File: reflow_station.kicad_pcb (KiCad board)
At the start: 6 copper layers, 180 x 110 mm, 271 parts, among them IC1 MP100LGN-Z, IC2 AMC23C10DWVR, J1 1731734, J10 USB_A, J11 USB_C_Receptacle_USB2.0_16P, J12 Conn_ARM_JTAG_SWD_10, J13 F52Q-1A7H1-11015, J2 1707027, J3 1707027, J4 1707027, J5 1707027, J6 DG301-5.0-02P-12-00A_H_, J7 DG301-5.0-02P-12-00A_H_, J8 DG301-5.0-02P-12-00A_H_, J9 DG301-5.0-02P-12-00A_H_, M1 Fan_CPU_4pin, M2 Fan_CPU_4pin, M3 Fan_CPU_4pin, M4 Fan_CPU_4pin, Q1 BTA16-600B, Q2 BTA16-600B, Q3 BTA16-600B, Q4 BTA16-600B, Q5 KSC1815YTA, SW2 SW_SPST, SW3 SW_SPST, SW4 SW_SPST, SW5 SW_DIP_x08, SW6 SW_Push, SW7 SW_SPDT, SW8 SW_SPDT, U1 TPS82130, U10 TPS2051BDBVR, U11 RCLAMP0504F.TCT, U12 RCLAMP0504F.TCT, U13 RCLAMP0504F.TCT, U14 STM32F469VIT6, U2 RAC20-12SK, U3 TPS82130, U4 MOC3052, U5 MOC3052, U6 MOC3052, U7 MOC3052, U8 ADS1118IDGS, U9 ADS1118IDGS, Y1 25MHz, Y2 32.768kHz

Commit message: feat: add board dimensions and change mcu position
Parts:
- removed the TP10 at (16.0, 199.0)
- removed the TP13 at (22.1, 195.9)
- removed the TP14 at (22.1, 199.0)
- removed the TP9 at (16.0, 195.9)
- TP1, TP2, TP3, TP4, TP5, TP6, TP7, TP8: moved to B.Cu
- TP10: renamed from TP12; moved to B.Cu
- TP11: renamed from TP15; moved to B.Cu
- TP12: renamed from TP16; moved to B.Cu
- TP13: renamed from TP17; moved to B.Cu
- TP14: renamed from TP18; moved to B.Cu
- TP15: renamed from TP19; moved to B.Cu
- TP16: renamed from TP20; moved to B.Cu
- TP17: renamed from TP21; moved to B.Cu
- TP18: renamed from TP22; moved to B.Cu
- TP19: renamed from TP23; moved to B.Cu
- TP20: renamed from TP24; moved to B.Cu
- TP21: renamed from TP25; moved to B.Cu
- TP22: renamed from TP26; moved to B.Cu
- TP23: renamed from TP27; moved to B.Cu
- TP24: renamed from TP28; moved to B.Cu
- TP25: renamed from TP29; moved to B.Cu
- TP26: renamed from TP30; moved to B.Cu
- TP27: renamed from TP31; moved to B.Cu
- TP28: renamed from TP32; moved to B.Cu
- TP29: renamed from TP33; moved to B.Cu
- TP30: renamed from TP34; moved to B.Cu
- TP31: renamed from TP35; moved to B.Cu
- TP32: renamed from TP36; moved to B.Cu
- TP33: renamed from TP37; moved to B.Cu
- TP34: renamed from TP38; moved to B.Cu
- TP35: renamed from TP39; moved to B.Cu
- TP36: renamed from TP40; moved to B.Cu
- TP9: renamed from TP11; moved to B.Cu
- moved J11 373.5 mm to (244.6, 76.3), turned to 90 degrees
- moved L2 370.4 mm to (238.5, 80.4)
- moved L1 366.9 mm to (235.2, 66.0)
- moved U12 364.0 mm to (236.7, 74.1), turned to 90 degrees
- moved R51 359.5 mm to (237.9, 77.4), turned to 90 degrees
- moved R50 357.3 mm to (235.9, 77.4), turned to 90 degrees
- moved R52 357.1 mm to (234.0, 73.9), turned to 90 degrees
- moved R49 355.2 mm to (233.9, 77.4), turned to 90 degrees
- moved C40 354.4 mm to (227.9, 57.8)
- moved L4 351.6 mm to (242.2, 48.2), turned to 90 degrees
- moved TP21 350.0 mm to (235.4, 63.6), turned to 180 degrees
- moved U10 348.4 mm to (228.0, 63.9)
- moved R74 347.2 mm to (233.2, 52.1), turned to 90 degrees
- moved C39 346.6 mm to (232.1, 62.2)
- moved C41 346.6 mm to (232.1, 64.1)
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- renumbered L5 to L4, L6 to L5, L4 to L6, R79 to R76, R76 to R77, R80 to R78, R77 to R79, R81 to R80, R78 to R81
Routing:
- net LINE: track 345.7 -> 331.7 mm
- net Net-(R16-Pad2): track 0.00 -> 3.31 mm
- net Net-(R15-Pad2): track 0.00 -> 3.00 mm
- net (no net): track 1.84 -> 0.00 mm
- net Net-(R20-Pad2): track 1.81 -> 0.00 mm

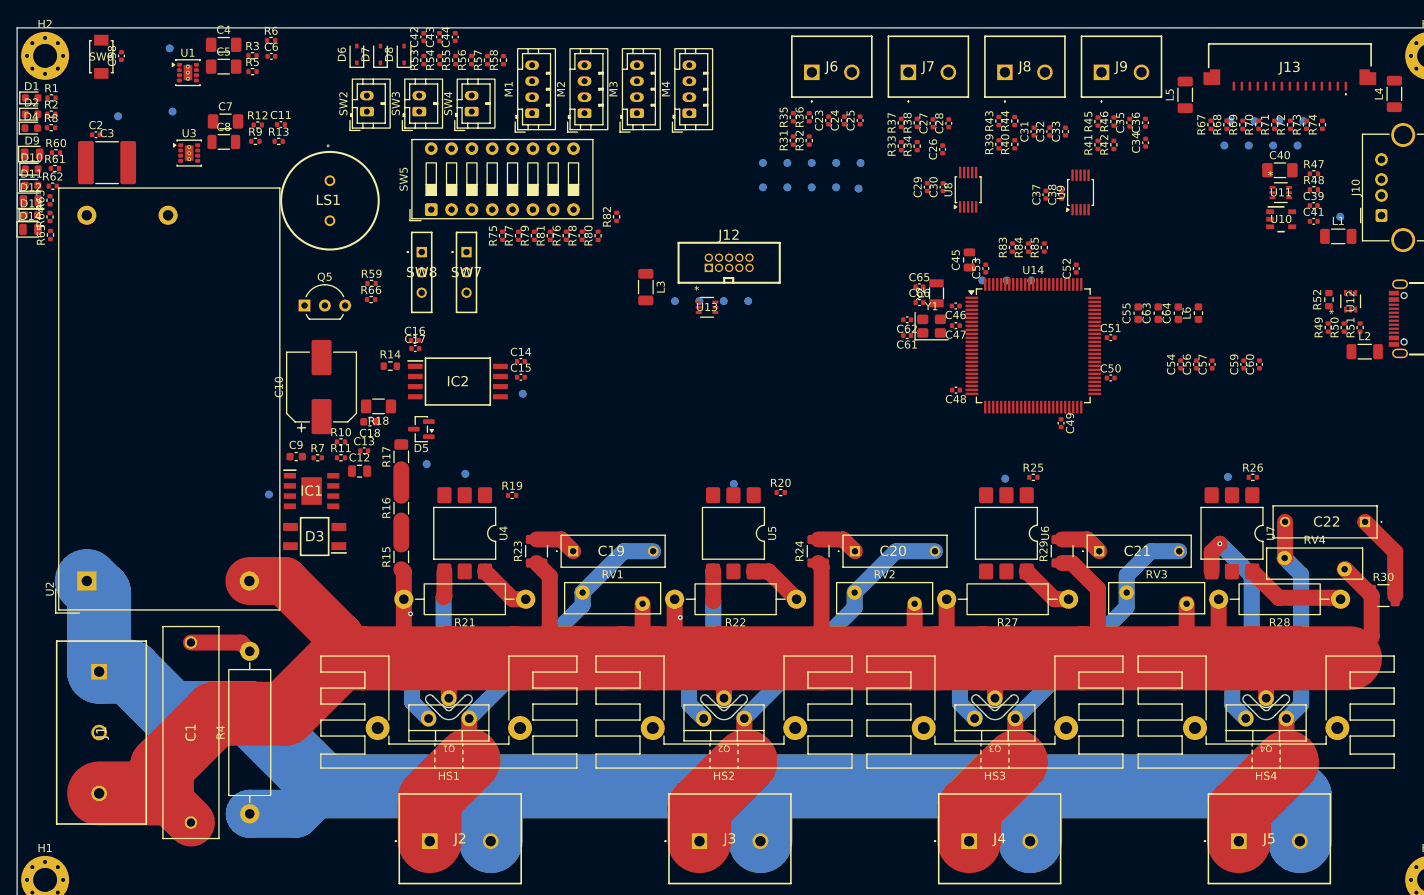
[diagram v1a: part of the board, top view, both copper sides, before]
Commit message: feat: add ground and earth(shield) planes, add better - multi layer connection for AC mains connector
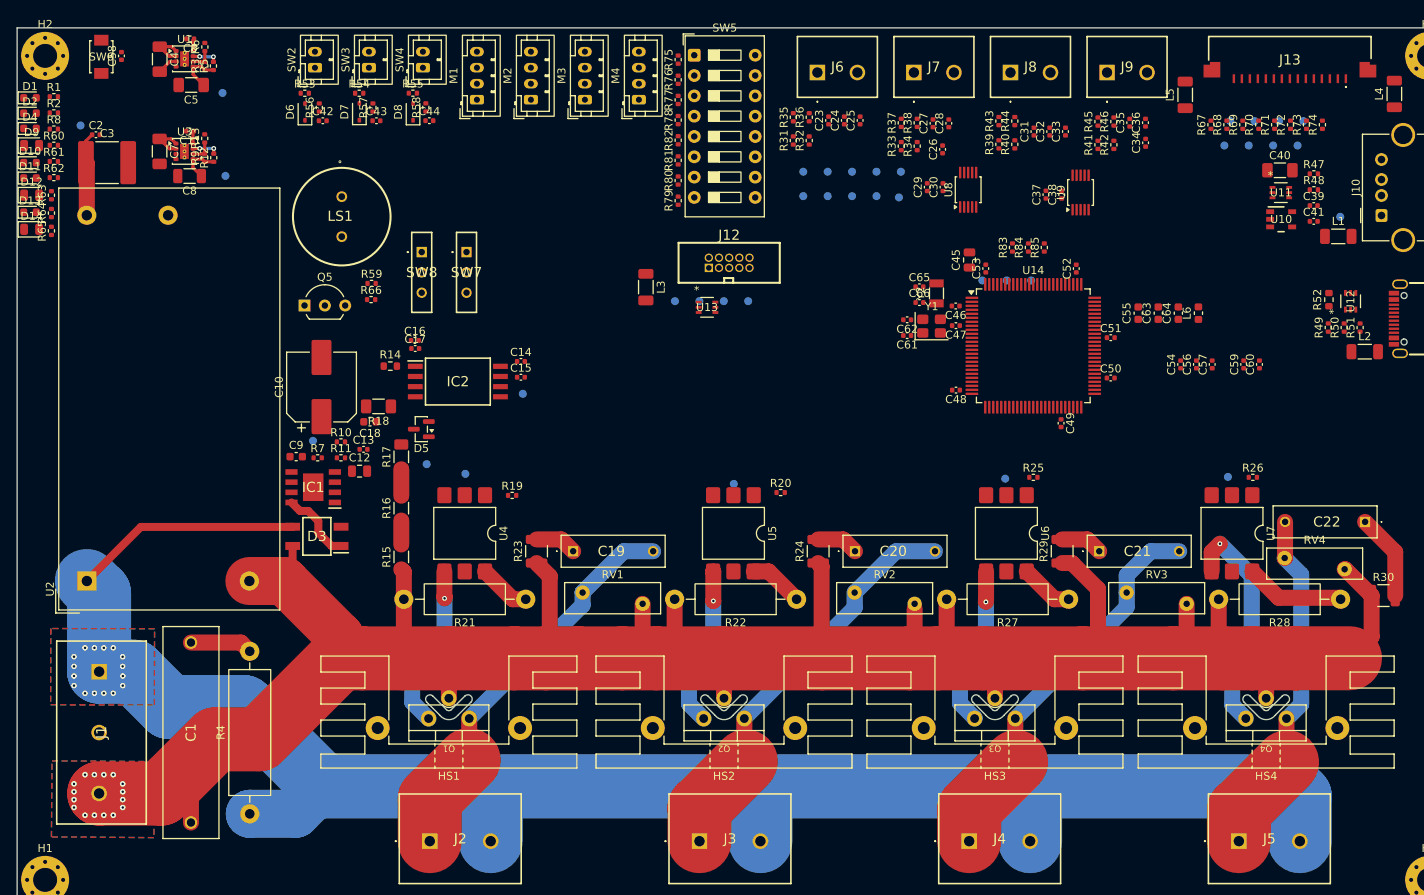
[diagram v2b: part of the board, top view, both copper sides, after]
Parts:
- moved SW5 38.1 mm to (154.7, 43.4), turned to 0 degrees
- moved R75 31.1 mm to (152.6, 43.9)
- moved R76 27.9 mm to (152.6, 46.4)
- moved R77 24.7 mm to (152.6, 49.0)
- moved R78 21.6 mm to (152.6, 51.5)
- moved R56 19.9 mm to (107.8, 49.9)
- moved C42 16.4 mm to (108.2, 51.6), turned to 0 degrees
- moved R57 15.5 mm to (114.5, 49.9)
- moved R53 15.4 mm to (106.0, 48.1), turned to 0 degrees
- moved R79 14.7 mm to (152.6, 61.6)
- moved R80 13.8 mm to (152.6, 59.0)
- moved R81 13.7 mm to (152.6, 56.5)
- moved C43 13.1 mm to (114.9, 51.6), turned to 0 degrees
- moved R82 12.3 mm to (152.6, 54.0)
- moved C11 11.4 mm to (91.6, 52.9), turned to 180 degrees
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- renumbered R77 to R76, R79 to R77, R81 to R78, R76 to R79, R78 to R80, R80 to R81
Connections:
- C12 pad 1: /Power/+12V_ISOLATED -> +12V_ISOLATED
- C13 pad 1: /Power/+12V_ISOLATED -> +12V_ISOLATED
- C9 pad 2: /Power/+12V_ISOLATED -> +12V_ISOLATED
- H3 pad 1: /SHIELD -> Earth
- H4 pad 1: /SHIELD -> Earth
- IC1 pad 4: /Power/+12V_ISOLATED -> +12V_ISOLATED
- R10 pad 1: /Power/+12V_ISOLATED -> +12V_ISOLATED
- R14 pad 1: /AC Synchronization/+12V_ISOLATED -> +12V_ISOLATED
- R7 pad 2: /Power/+12V_ISOLATED -> +12V_ISOLATED
- TP4 pad 1: /Power/+12V_ISOLATED -> +12V_ISOLATED
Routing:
- net NEUT: track 216.6 -> 245.1 mm, vias 0 -> 16
- net +12V: track 0.00 -> 20.1 mm
- net Net-(Q3-G): track 7.11 -> 20.5 mm, vias 0 -> 1
- net /Power/L_RECTIFIED: track 0.00 -> 9.31 mm
- net +5V: track 0.00 -> 5.56 mm
- net +3V3: track 0.00 -> 5.28 mm
- net LINE: track 331.7 -> 335.5 mm, vias 2 -> 16
- net Net-(U3-PG): track 0.00 -> 3.26 mm, vias 0 -> 2
- net Net-(U1-PG): track 0.00 -> 3.20 mm, vias 0 -> 2
- net Net-(U3-FB): track 0.00 -> 2.87 mm
- net Net-(U1-FB): track 0.00 -> 2.84 mm
- net GND: track 0.00 -> 2.58 mm
- net Net-(U3-SS/TR): track 0.00 -> 1.60 mm
- net Net-(U1-SS/TR): track 0.00 -> 1.56 mm
- net Net-(Q1-G): vias 0 -> 1
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- added copper zone on In4.Cu, net GND
- added copper zone on B.Cu, net LINE
- added copper zone on F.Cu, net LINE
- added copper zone on In1.Cu, net LINE
- added copper zone on In2.Cu, net LINE
- added copper zone on In3.Cu, net LINE
- added copper zone on In4.Cu, net LINE
- added copper zone on B.Cu, net NEUT
- added copper zone on F.Cu, net NEUT
- added copper zone on In1.Cu, net NEUT
- added copper zone on In2.Cu, net NEUT
- added copper zone on In3.Cu, net NEUT
- added copper zone on In4.Cu, net NEUT
- removed copper zone on In1.Cu, net GND1

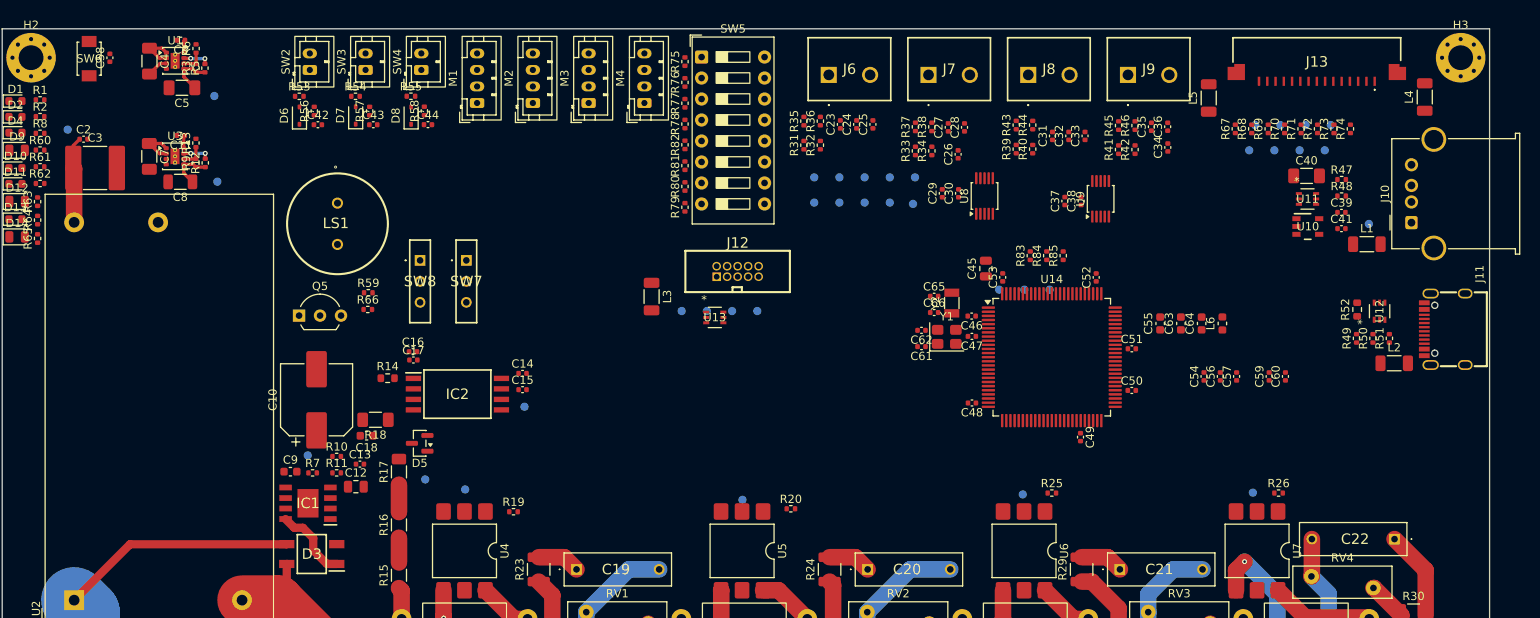
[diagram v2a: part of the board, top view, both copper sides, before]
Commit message: feat: add power planes and move voltage regulators closer to their usage
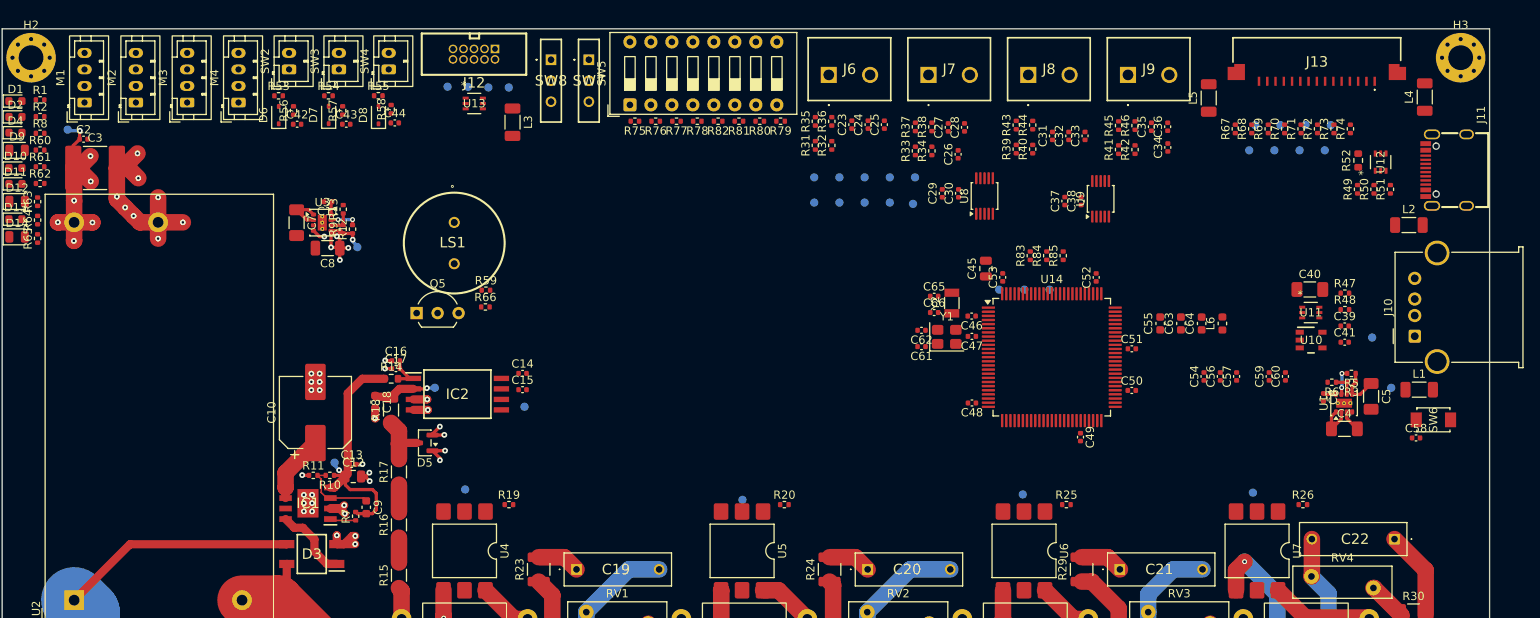
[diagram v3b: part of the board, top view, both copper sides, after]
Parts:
- R19, R20, R25, R26: value 680 -> 220
- moved SW6 168.4 mm to (243.2, 87.3), turned to 180 degrees
- moved C58 164.6 mm to (241.1, 89.5), turned to 0 degrees
- moved C4 151.3 mm to (232.4, 88.4), turned to 0 degrees
- moved C5 148.7 mm to (235.7, 84.4), turned to -90 degrees
- moved U1 147.4 mm to (232.4, 85.3), turned to 90 degrees
- moved TP1 146.7 mm to (238.1, 83.4), turned to -90 degrees
- moved R3 144.9 mm to (233.3, 82.7), turned to 180 degrees
- moved C6 144.9 mm to (229.9, 84.6), turned to -90 degrees
- moved R5 143.6 mm to (233.3, 81.7), turned to 180 degrees
- moved R6 143.3 mm to (230.9, 82.7), turned to 180 degrees
- moved M4 49.1 mm to (98.6, 48.9)
- moved M3 48.6 mm to (92.4, 48.9)
- moved M2 48.0 mm to (86.2, 48.9)
- moved M1 47.5 mm to (80.0, 48.9)
- moved TP25 44.3 mm to (126.4, 47.0)
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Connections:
- R19 pad 1: +5V -> +3V3
- R20 pad 1: +5V -> +3V3
- R25 pad 1: +5V -> +3V3
- R26 pad 1: +5V -> +3V3
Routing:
- net +12V_ISOLATED: track 0.00 -> 30.7 mm, vias 0 -> 1
- net GND1: track 0.00 -> 26.1 mm, vias 0 -> 30
- net GND: track 2.58 -> 26.8 mm, vias 0 -> 8
- net +12V: track 20.1 -> 34.6 mm, vias 0 -> 7
- net +3V3: track 5.28 -> 15.3 mm, vias 0 -> 6
- net Net-(IC1-FB): track 0.00 -> 9.12 mm
- net Net-(IC1-VB): track 0.00 -> 8.15 mm
- net Net-(IC2-INP): track 0.00 -> 7.78 mm, vias 0 -> 1
- net Net-(D5-COM): track 0.00 -> 7.01 mm
- net Net-(IC2-VDD1): track 0.00 -> 4.96 mm
- net Net-(IC1-PG): track 0.00 -> 3.13 mm
- added copper zone on In2.Cu, net +12V
- added copper zone on In2.Cu, net +3V3
- added copper zone on In1.Cu, net GND1
- added copper zone on In4.Cu, net GND1

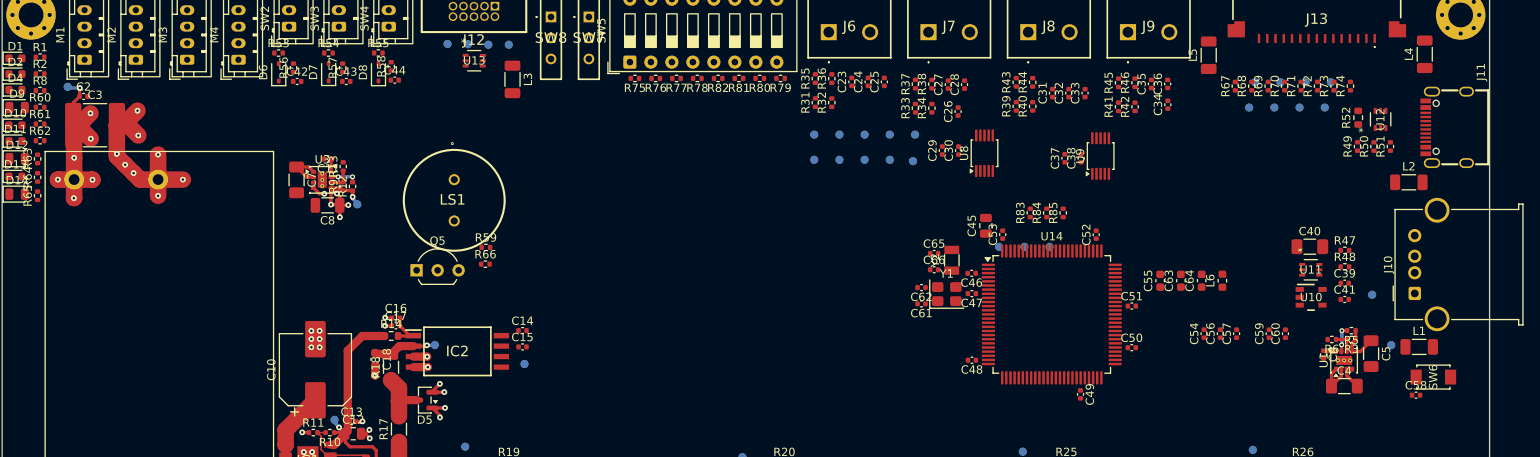
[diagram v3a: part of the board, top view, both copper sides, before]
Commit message: feat: route USB differential traces
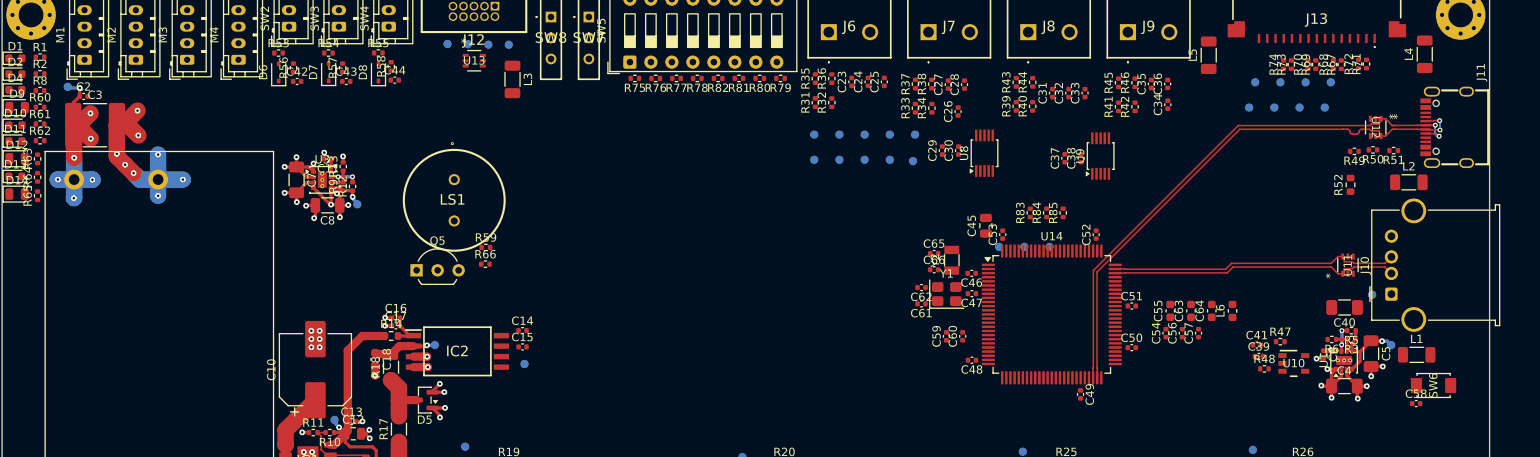
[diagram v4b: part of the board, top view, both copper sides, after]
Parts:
- moved C59 39.1 mm to (184.3, 82.3)
- moved C60 39.1 mm to (186.2, 82.3)
- moved R48 15.7 mm to (222.8, 86.3)
- moved C39 13.7 mm to (222.1, 84.8)
- moved R47 13.5 mm to (224.7, 83.0)
- moved R67 13.1 mm to (232.1, 49.5)
- moved C41 12.0 mm to (221.8, 83.4)
- moved R68 10.2 mm to (231.1, 49.5)
- moved R74 8.50 mm to (225.1, 49.5)
- moved C40 8.47 mm to (232.5, 78.9), turned to 180 degrees
- moved R71 8.35 mm to (235.1, 49.4)
- moved U10 8.27 mm to (226.3, 85.6)
- moved R52 8.18 mm to (233.2, 64.0)
- moved R69 6.31 mm to (229.0, 49.5)
- moved R73 5.78 mm to (226.0, 49.5)
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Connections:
- C29 pad 1: +5V -> +3V3
- C30 pad 1: +5V -> +3V3
- C37 pad 1: +5V -> +3V3
- C38 pad 1: +5V -> +3V3
- R31 pad 2: +5V -> +3V3
- R33 pad 2: +5V -> +3V3
- R39 pad 2: +5V -> +3V3
- R41 pad 2: +5V -> +3V3
- U8 pad 8: +5V -> +3V3
- U9 pad 8: +5V -> +3V3
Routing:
- net /Connectivity/USB_UART_D-: track 0.00 -> 66.1 mm, vias 0 -> 2
- net /Connectivity/USB_UART_D+: track 0.00 -> 66.1 mm, vias 0 -> 2
- net /Connectivity/USB_D+: track 0.00 -> 35.1 mm
- net /Connectivity/USB_D-: track 0.00 -> 35.1 mm
- net GND: track 26.8 -> 42.4 mm, vias 8 -> 19
- net +12V: track 34.6 -> 41.9 mm, vias 7 -> 13
- net +5V: track 5.56 -> 10.7 mm, vias 0 -> 1
- net +3V3: track 15.3 -> 16.7 mm, vias 6 -> 5
